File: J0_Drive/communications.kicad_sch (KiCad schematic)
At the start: 11 parts, among them J4 Conn_01x02, J5 Conn_01x02, J6 Conn_01x03, J7 Conn_01x03, J9 Conn_ARM_JTAG_SWD_10, U3 TJA1051TK-3

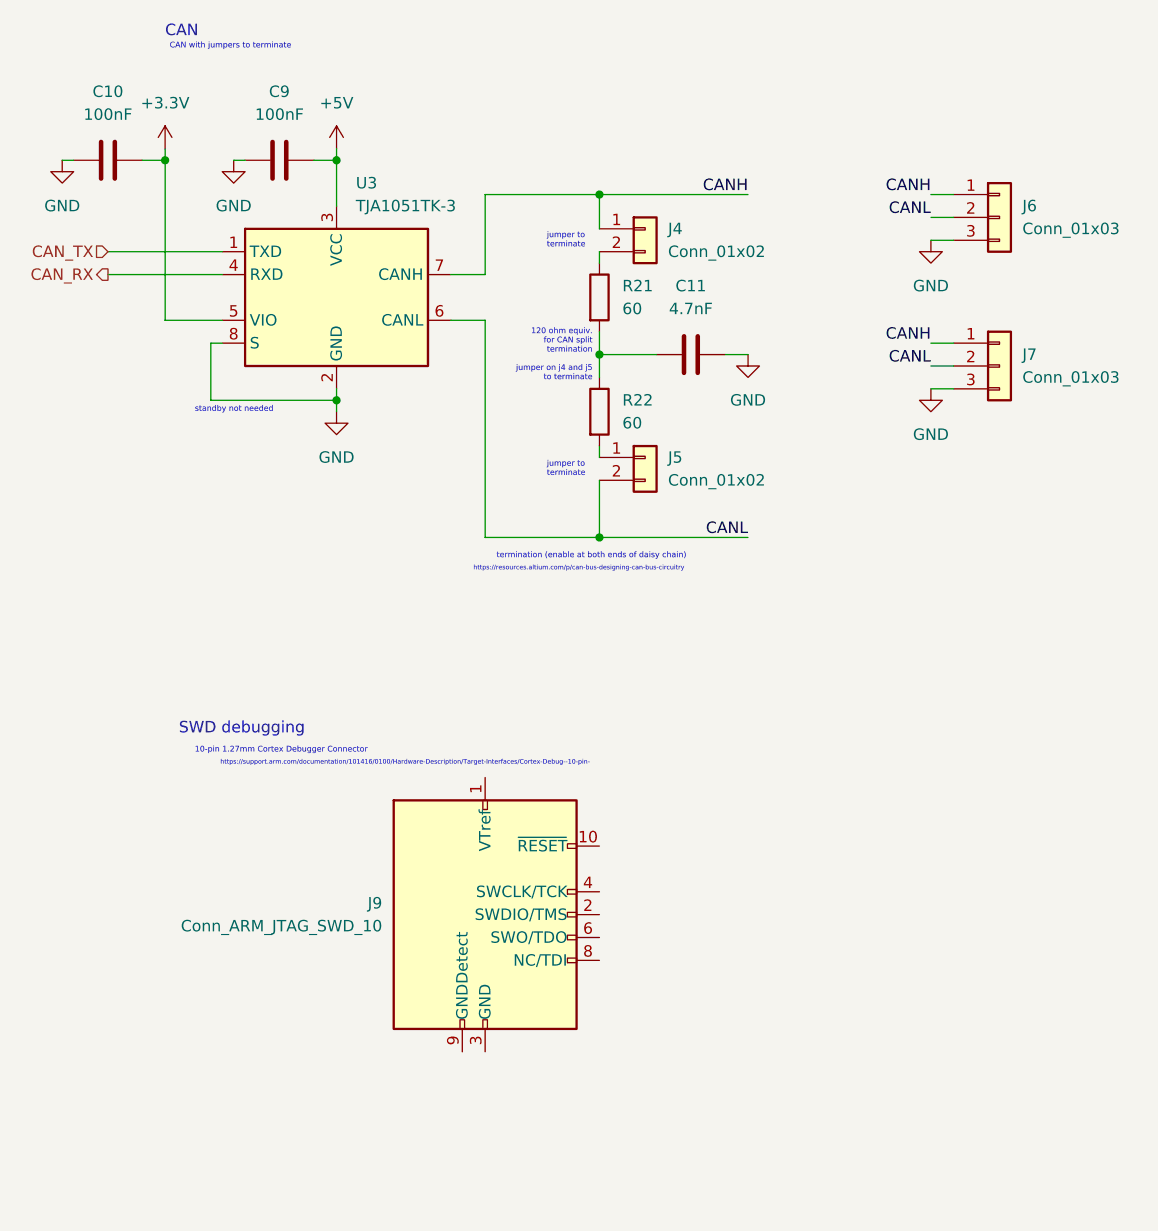
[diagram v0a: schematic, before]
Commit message: organized hierarchical sheets, finished communications, started sensors
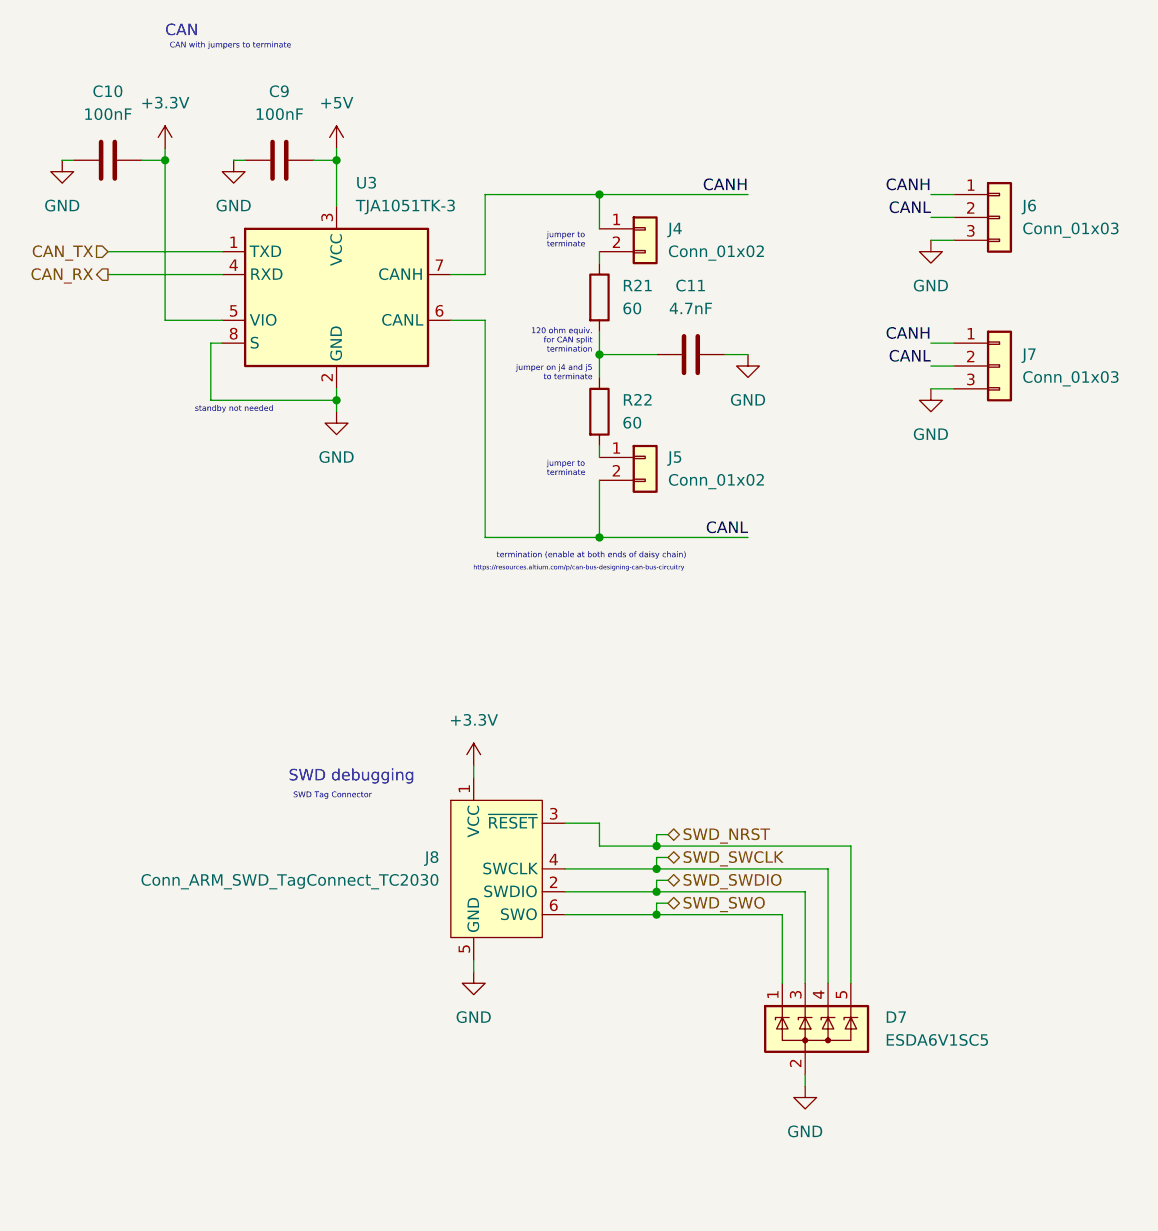
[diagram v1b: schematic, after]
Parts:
- removed J9: Conn_ARM_JTAG_SWD_10, symbol Connector:Conn_ARM_JTAG_SWD_10
- added D7: ESDA6V1SC5, Package_TO_SOT_SMD:SOT-23-5, symbol Power_Protection:ESDA6V1SC5
- added J8: Conn_ARM_SWD_TagConnect_TC2030, Connector:Tag-Connect_TC2030-IDC-FP_2x03_P1.27mm_Vertical, symbol Connector:Conn_ARM_SWD_TagConnect_TC2030
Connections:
- net +3.3V: now also J8.1 (VCC)
- net GND: now also D7.2 (A), J8.5 (GND)
- new net SWD_NRST: D7.5 (K), J8.3 (~{RESET})
- new net SWD_SWCLK: D7.4 (K), J8.4 (SWCLK)
- new net SWD_SWDIO: D7.3 (K), J8.2 (SWDIO)
- new net SWD_SWO: D7.1 (K), J8.6 (SWO)
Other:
- note added: "SWD Tag Connector"
- note removed: "10-pin 1.27mm Cortex Debugger Connector"
- note removed: "https://support.arm.com/documentation/101416/0100/Hardware-Description/Target-Interfaces/Cortex-Debug--10-pin-"

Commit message: finished comms SWD header, main page organization
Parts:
- removed D7: ESDA6V1SC5, Package_TO_SOT_SMD:SOT-23-5, symbol Power_Protection:ESDA6V1SC5
- removed J8: Conn_ARM_SWD_TagConnect_TC2030, Connector:Tag-Connect_TC2030-IDC-FP_2x03_P1.27mm_Vertical, symbol Connector:Conn_ARM_SWD_TagConnect_TC2030
- added J8: Conn_02x05_Odd_Even, symbol Connector_Generic:Conn_02x05_Odd_Even
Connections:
- net +3.3V: now also J8.1 (Pin_1)
- net GND: now also J8.3 (Pin_3), J8.5 (Pin_5), J8.9 (Pin_9)
- net SWD_NRST: now also J8.10 (Pin_10)
- net SWD_SWCLK: now also J8.4 (Pin_4)
- net SWD_SWDIO: now also J8.2 (Pin_2)
- net SWD_SWO: now also J8.6 (Pin_6)
- no-connect marks 0 -> 2
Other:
- note added: "Cortex Debug 10-pin Connector"
- note removed: "SWD Tag Connector"
